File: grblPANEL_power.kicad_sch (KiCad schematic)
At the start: 24 parts, among them J101 Conn_01x02, U101 MAX17612A, U102 AZ1117-3.3

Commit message: Power protection status LEDs - wip
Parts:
- removed TP101, TP102: TestPoint, TestPoint:TestPoint_THTPad_D2.0mm_Drill1.0mm, symbol Connector:TestPoint
- added C?: 22u, Capacitor_SMD:C_0805_2012Metric, symbol Device:C
- added D?: 3.9v Zener, symbol Device:D_Zener
- added D?: D_Schottky, Diode_SMD:D_SOD-323, symbol Device:D_Schottky
- added D? (x2): LED, LED_SMD:LED_0603_1608Metric, symbol Device:LED
- added Q501: Q_NPN_BEC - S8050, Package_TO_SOT_SMD:SOT-23, symbol Device:Q_NPN_BEC
- added R? (x2): 1k, Resistor_SMD:R_0603_1608Metric, symbol Device:R
- added R?: 6k8, Resistor_SMD:R_0603_1608Metric, symbol Device:R
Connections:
- net FLAG: now also R?.2
- net GND: now also C?.2, D?.2 (A)
- net UVOV: now also R?.2
- net VIN: now also D?.2 (A)
- new net: C?.1, D?.1 (K), Q501.1 (B), R?.2
- new net: D?.2 (A), D?.2 (A), Q501.2 (E)
- new net: D?.1 (K), Q501.3 (C), R?.1
- new net: D?.1 (K), R?.1 (x2)
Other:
- note added: "FLAG and UVOV status pins are open drain, max voltage ~6v Zener/transistor circuit to generate ~3.3v from unprotected input supply"
- note added: "Power protection status LEDs"
- note added: "todo: power leds - confirm suitable resistor & capacitor values after testing"
- note removed: "todo: power led - confirm resistor value once led known"

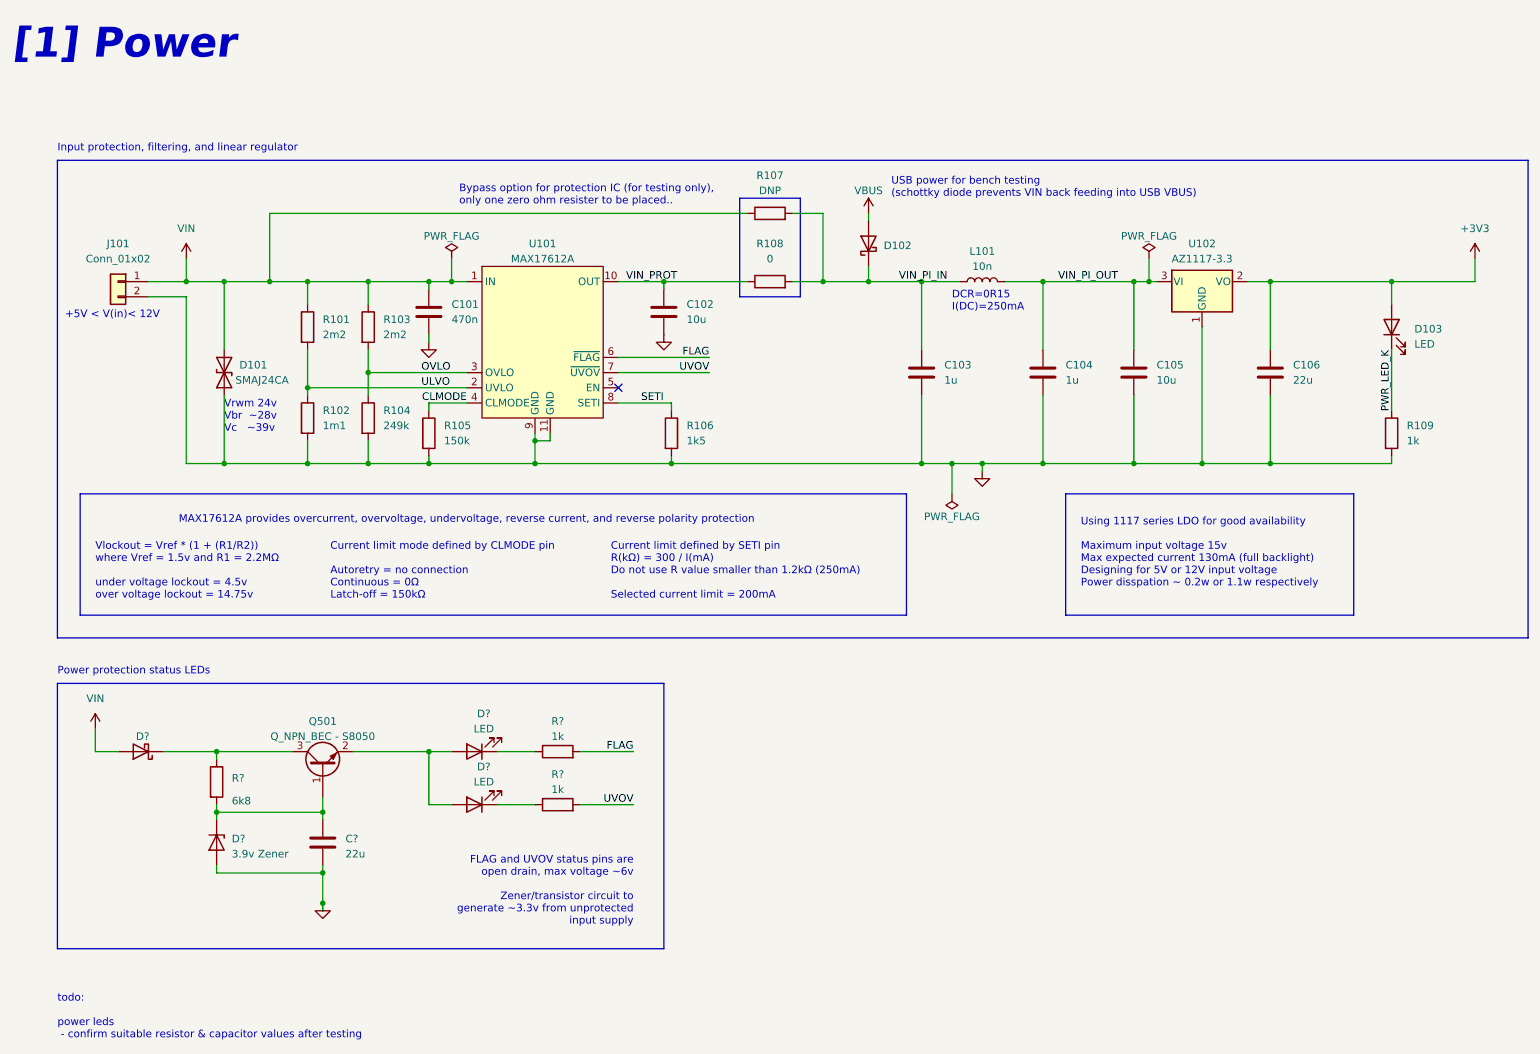
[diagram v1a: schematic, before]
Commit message: More power protect status LED work
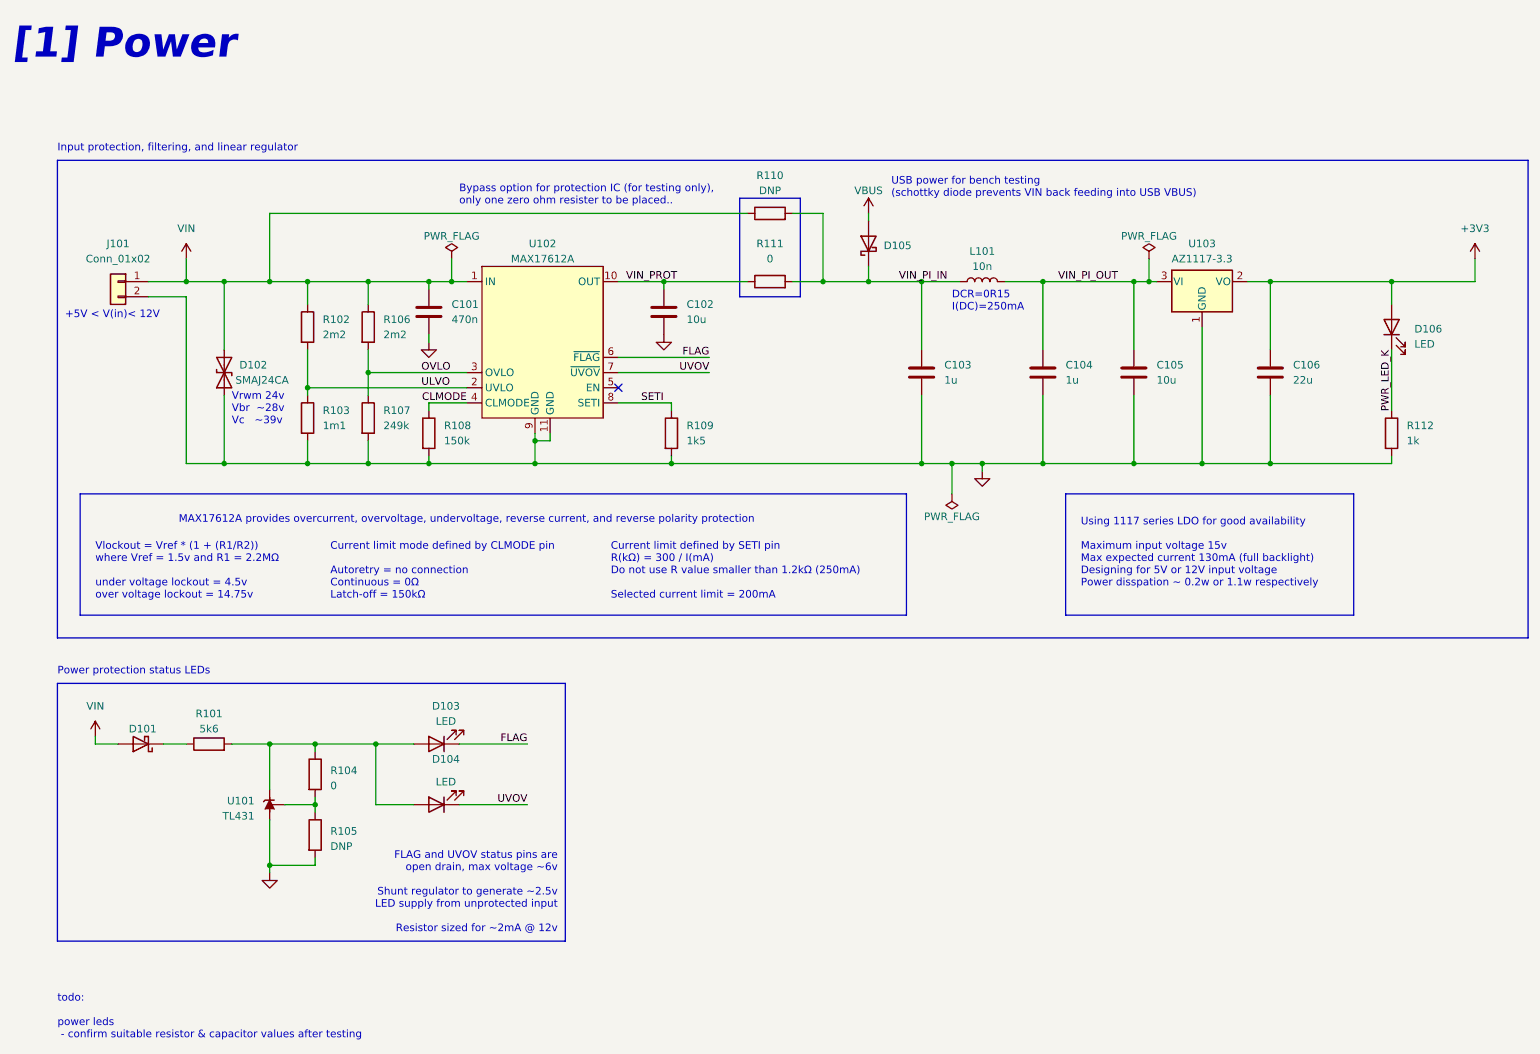
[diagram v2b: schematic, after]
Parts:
- removed C?: 22u, Capacitor_SMD:C_0805_2012Metric, symbol Device:C
- removed D?: 3.9v Zener, symbol Device:D_Zener
- removed Q501: Q_NPN_BEC - S8050, Package_TO_SOT_SMD:SOT-23, symbol Device:Q_NPN_BEC
- removed R? (x2): 1k, Resistor_SMD:R_0603_1608Metric, symbol Device:R
- removed R?: 6k8, Resistor_SMD:R_0603_1608Metric, symbol Device:R
- added R101: 5k6, Resistor_SMD:R_0603_1608Metric, symbol Device:R
- added R104: 0, Resistor_SMD:R_0603_1608Metric, symbol Device:R
- added R105: DNP, Resistor_SMD:R_0603_1608Metric, symbol Device:R
- added U101: TL431, Package_TO_SOT_SMD:SOT-23, symbol Reference_Voltage:TL431DBZ
- D103, D104: renamed from D?; footprint LED_SMD:LED_0603_1608Metric -> LED_SMD:LED_1206_3216Metric_ReverseMount_Hole1.8x2.4mm
- D106: renamed from D103; footprint LED_SMD:LED_0603_1608Metric -> LED_SMD:LED_1206_3216Metric_ReverseMount_Hole1.8x2.4mm
- gave numbers to parts that had none: 1
- renumbered D101 to D102, D102 to D105, R101 to R102, R102 to R103, R103 to R106, R104 to R107, R105 to R108, R106 to R109, R107 to R110, R108 to R111, R109 to R112, U101 to U102, U102 to U103
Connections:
- net FLAG: now also D103.1 (K)
- net GND: now also R105.2, U101.3 (A)
- net UVOV: now also D104.1 (K)
- net at D103.2 (A), D104.2 (A): now also R101.2, R104.1, U101.1 (K)
- net at D101.1 (K): now also R101.1
- new net: R104.2, R105.1, U101.2 (REF)
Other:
- note added: "FLAG and UVOV status pins are open drain, max voltage ~6v Shunt regulator to generate ~2.5v LED supply from unprotected input Resistor sized for ~2mA @ 12v"
- note removed: "FLAG and UVOV status pins are open drain, max voltage ~6v Zener/transistor circuit to generate ~3.3v from unprotected input supply"
- moved on the sheet: D101, D103, D104
